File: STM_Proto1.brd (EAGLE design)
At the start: 160 x 100 mm, 81 parts, among them IC1 LM358D, Q1 8M, Q2 32748

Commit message: Libraries for Simholder and HM-10
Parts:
- removed SV1: (no value), con-lstb:MA03-1
- removed U$1: SIMHOLDER3, SparkFun-Connectors:SIMHOLDER3
- added E1: HM-10-BOARD, JNHuaMao:26.9X13X2.2_BOARD
- added LED4: (no value), led:CHIPLED_1206
- added R26, R27: 470, resistor:R0805
- added R28: reset, resistor:R1206
- added U$3: SIMHOLDER3, SparkFun-Connectors:SIMHOLDER3
- moved IC1 97.8 mm to (-24.1, 63.5)
- moved LED1 77.7 mm to (-94.0, 102.9)
- moved C18 71.4 mm to (-16.5, 99.1)
- moved C19 71.4 mm to (-21.6, 99.1)
- moved C10 10.2 mm to (-72.4, 92.7)
- moved R2 10.2 mm to (-47.0, 99.1)
- moved R4 10.2 mm to (-52.1, 99.1)
- moved T1 10.2 mm to (-66.0, 97.8)
- moved T2 10.2 mm to (-71.1, 97.8)
- moved R18 10.2 mm to (-26.7, 99.1)
- moved R3 10.2 mm to (-31.8, 99.1)
- moved C14 10.2 mm to (-77.5, 92.7)
- moved C15 10.2 mm to (-82.5, 92.7)
- moved C16 10.2 mm to (-87.6, 92.7)
- moved C17 10.2 mm to (-92.7, 92.7)
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- renumbered JP2 to JP1
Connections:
- removed net +3V3: SV1.3
- removed net A0.0+: IC1.1, R25.1, SV1.1
- removed net ADC_RES: STM32L152CBT6.18
- new net ADC_TERM: IC1.1, R25.1, STM32L152CBT6.18
- new net I2C_SCL: JP1.3, STM32L152CBT6.42
- new net I2C_SDA: JP1.4, STM32L152CBT6.43
- new net N$26: E1.24, R26.2
- new net N$27: LED4.A, R26.1
- new net N$37: E1.23, R27.2, R28.2
- net 3.3V: now also E1.12, JP1.1, R27.1
- net CTS: no longer JP1.1
- net DCD: no longer JP1.4
- net DTR: no longer JP1.3
- net GND: now also E1.13, E1.14, E1.21, E1.22, JP1.2, LED4.C, R28.1, U$3.6; no longer SV1.2, U$1.6
- net N$10: now also U$3.1; no longer U$1.1
- net N$14: now also U$3.2; no longer U$1.2
- net N$16: now also U$3.3; no longer U$1.3
- net N$18: now also U$3.4; no longer U$1.4
- net RTS: no longer JP1.2
- net USART2_RX: now also E1.1
- net USART2_TX: now also E1.2

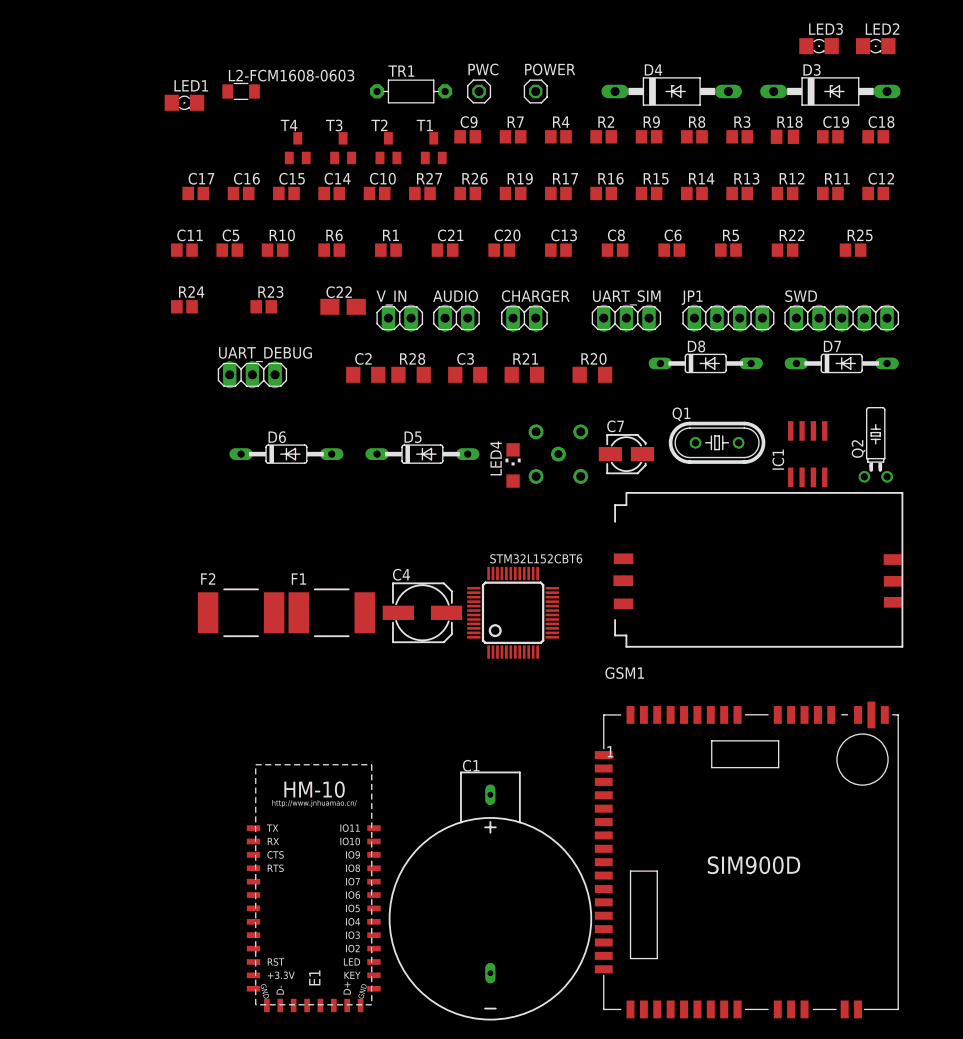
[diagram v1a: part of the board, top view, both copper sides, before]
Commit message: Add Charger
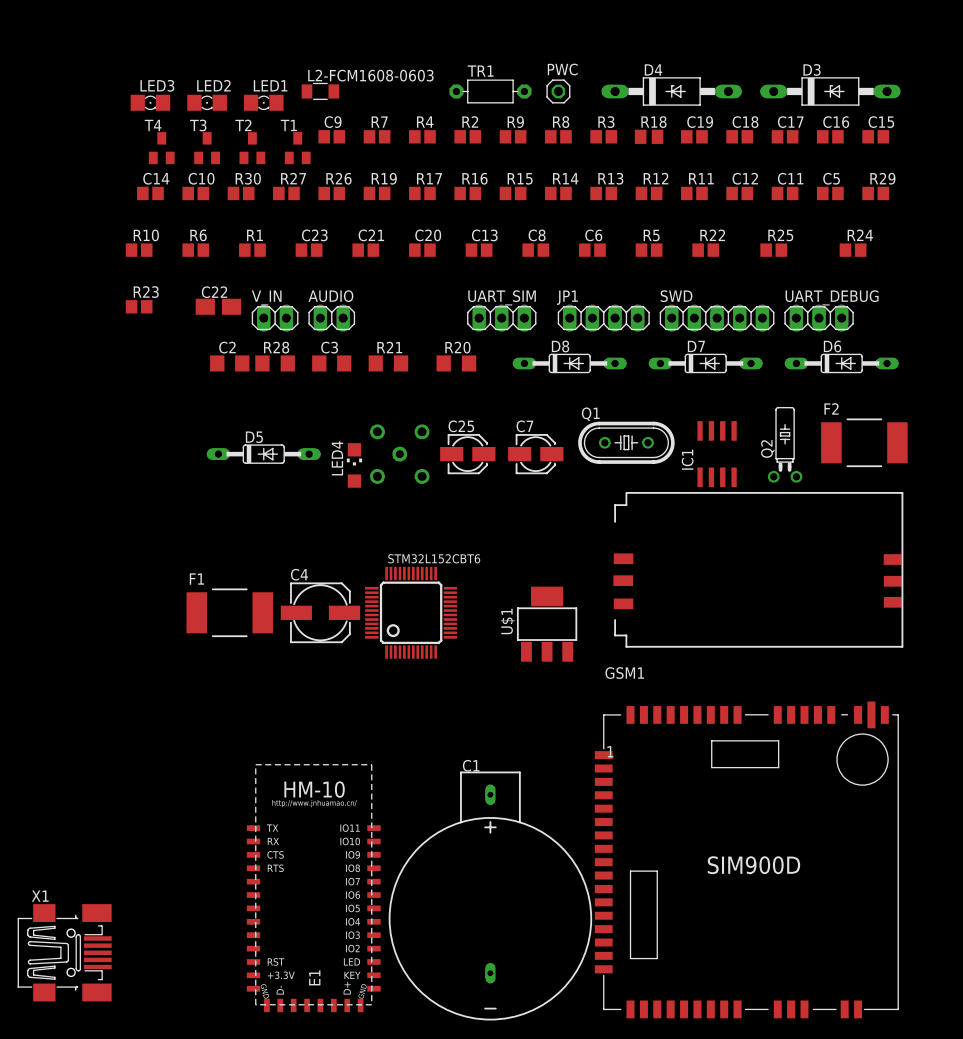
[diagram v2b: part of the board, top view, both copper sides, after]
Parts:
- removed CHARGER: (no value), pinhead:1X02
- removed POWER: (no value), pinhead:1X01
- added C23: 100n, resistor:C0805
- added C25: 10u, resistor:153CLV-0405
- added R29: 4.7k, resistor:R0805
- added R30: 15k, resistor:R0805
- added U$1: LD1117AS33, LD1117AS33:SOT223
- added X1: MINI-USB-32005-201, con-cypressindustries:32005-201
- moved LED3 75.2 mm to (-97.8, 102.9)
- moved R24 75.2 mm to (-19.1, 86.4)
- moved LED2 75.2 mm to (-91.4, 102.9)
- moved F2 72.4 mm to (-17.8, 64.8)
- moved C11 67.6 mm to (-26.7, 92.7)
- moved C5 67.6 mm to (-21.6, 92.7)
- moved C15 66.3 mm to (-16.5, 99.1)
- moved C16 66.3 mm to (-21.6, 99.1)
- moved C17 66.3 mm to (-26.7, 99.1)
- moved UART_DEBUG 63.8 mm to (-22.9, 78.7)
- moved D6 63.1 mm to (-20.3, 73.7)
- moved C14 20.3 mm to (-97.8, 92.7)
- moved C10 20.3 mm to (-92.7, 92.7)
- moved LED4 17.8 mm to (-74.9, 62.2)
- moved D5 17.8 mm to (-85.1, 63.5)
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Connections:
- removed net N$21: CHARGER.2, GSM1.28
- removed net N$6: POWER.1, R10.1
- new net ADC_BAT: R29.2, R30.1, STM32L152CBT6.19
- new net POWER: R10.1, STM32L152CBT6.14
- new net USB+: GSM1.28, X1.1
- net 3.3V: now also C25.+, LED1.A, LED2.A, R16.2, T4.E, U$1.2, U$1.TAB; no longer V_IN.1
- net GND: now also C23.2, C25.-, R30.2, U$1.1, X1.5
- net N$20: no longer CHARGER.1
- net V_IN: now also C23.1, R29.1, U$1.3, V_IN.1; no longer LED1.A, LED2.A, R16.2, T4.E

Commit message: Last version with SIM900D
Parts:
- removed AUDIO: (no value), pinhead:1X02
- removed C18, C19: 33p, resistor:C0805
- removed C22: 1u, resistor:A/3216-18W
- removed C23: 100n, resistor:C0805
- removed C25: 10u, resistor:153CLV-0405
- removed C4: 100u, resistor:153CLV-0605
- removed D3, D4: (no value), diode:F126Z12
- removed E1: HM-10-BOARD, JNHuaMao:26.9X13X2.2_BOARD
- removed JP1: (no value), pinhead:1X04
- removed LED4: (no value), led:CHIPLED_1206
- removed PWC: (no value), pinhead:1X01
- removed R28: reset, resistor:R1206
- removed U$1: LD1117AS33, LD1117AS33:SOT223
- added I2C1, I2C2, I2C3: (no value), pinhead:1X04
- added LED10: (no value), led:CHIPLED_1206
- added R31: 10k, resistor:M0805
- added R31-TEMP: NCP15XH103F03RC, resistor:M0805
- added R32: 10, resistor:M0805
- added R33: RESET_HC, resistor:M0805
- added S1: SWS002, smd-special:SMS-002
- added U$4: (no value), hc-05 eagle lib:BTM400_6B
- added U$5: MIC29302WT, MIC29302WT:TO263-5
- added V_IN1: (no value), pinhead:1X02
- C14: value 10p -> 100u; device resistor:C0805 -> resistor:153CLV-0807
- C15: value 33p -> 22u; device resistor:C0805 -> resistor:153CLV-0605
- C16, C17: value 10p -> 10u; device resistor:C0805 -> resistor:153CLV-0505
- C3: device resistor:C1206 -> resistor:C0805
- C7: value 10u -> 1u
- R26, R27: value 470 -> 4.7k
- moved R23 192.4 mm to (88.2, 35.6), flipped to the bottom, turned to 180 degrees
- moved C14 178.2 mm to (79.3, 72.7), flipped to the bottom
- moved C10 177.5 mm to (74.3, 32.6), flipped to the bottom
- moved L2-FCM1608-0603 174.7 mm to (74.7, 20.5), flipped to the bottom, turned to 270 degrees
- moved F1 173.0 mm to (83.1, 27.7), flipped to the bottom, turned to 270 degrees
- moved R10 170.0 mm to (57.6, 20.4), flipped to the bottom, turned to 270 degrees
- moved C9 167.1 mm to (74.3, 29.0), flipped to the bottom
- moved C21 162.0 mm to (78.0, 29.4), flipped to the bottom, turned to 90 degrees
- moved R27 160.0 mm to (74.9, 64.4), flipped to the bottom, turned to 270 degrees
- moved R26 158.5 mm to (78.5, 64.4), flipped to the bottom, turned to 90 degrees
- moved T3 154.7 mm to (63.0, 87.9), flipped to the bottom
- moved R5 144.3 mm to (88.5, 24.8), flipped to the bottom, turned to 270 degrees
- moved TR1 139.0 mm to (69.8, 53.5), turned to 270 degrees
- moved T4 138.6 mm to (41.1, 81.2), flipped to the bottom
- moved LED3 136.9 mm to (37.7, 83.7), flipped to the bottom, turned to 270 degrees
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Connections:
- removed net N$26: E1.24, R26.2
- removed net N$27: LED4.A, R26.1
- removed net N$37: E1.23, R27.2, R28.2
- removed net N$7: GSM1.47, PWC.1
- new net N$21: R32.1, U$4.PIO(1)
- new net N$33: LED10.A, R32.2
- new net N$38: R26.2, R27.1, U$5.5
- new net N$6: R31.1, R33.1, U$4.RESETB
- new net VBAT@2: GSM1.38, GSM1.39, S1.1, S1.2
- net 3.3V: now also C14.+, C15.+, C16.+, I2C1.1, I2C2.1, I2C3.1, R26.1, R31.2, S1.4, U$4.3.3V, U$5.4, V_IN1.1; no longer C25.+, C4.+, C7.+, E1.12, GSM1.38, GSM1.39, JP1.1, R27.1, U$1.2, U$1.TAB
- net GND: now also C14.-, C15.-, C16.-, C17.-, I2C1.2, I2C2.2, I2C3.2, LED10.C, R27.2, R31-TEMP.2, R33.2, U$4.GND@1, U$4.GND@2, U$4.GND@3, U$4.GND@4, U$5.3, V_IN1.2; no longer C14.1, C15.1, C17.2, C18.2, C22.-, C23.2, C25.-, C4.-, D3.C, D4.A, E1.13, E1.14, E1.21, E1.22, JP1.2, LED4.C, R28.1, U$1.1
- net I2C_SCL: now also I2C1.3, I2C2.3, I2C3.3; no longer JP1.3
- net I2C_SDA: now also I2C1.4, I2C2.4, I2C3.4; no longer JP1.4
- net N$20: now also R31-TEMP.1
- net N$31: now also C7.+; no longer C22.+
- net OUT+: no longer AUDIO.2, C16.2, C17.1, C18.1, C19.2, D4.C
- net OUT-: no longer AUDIO.1, C14.2, C15.2, C16.1, C19.1, D3.A
- net USART2_RX: now also U$4.UART-RX; no longer E1.1
- net USART2_TX: now also U$4.UART-TX; no longer E1.2
- net V_IN: now also C17.+, S1.3, U$5.1, U$5.2; no longer C23.1, U$1.3
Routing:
- net GND: track 0.00 -> 803.2 mm, vias 0 -> 6
- net 3.3V: track 0.00 -> 505.1 mm, vias 0 -> 10
- net V_IN: track 0.00 -> 348.0 mm, vias 0 -> 4
- net USART2_TX: track 0.00 -> 332.7 mm, vias 0 -> 4
- net USART2_RX: track 0.00 -> 325.2 mm, vias 0 -> 2
- net N$1: track 0.00 -> 201.5 mm, vias 0 -> 2
- net NRST: track 0.00 -> 129.2 mm, vias 0 -> 6
- net DEB_TX: track 0.00 -> 128.4 mm
- net DEB_RX: track 0.00 -> 108.1 mm
- net PWRK: track 0.00 -> 93.5 mm
- net ADC_BAT: track 0.00 -> 87.8 mm
- net I2C_SDA: track 0.00 -> 85.3 mm, vias 0 -> 4
- net RING: track 0.00 -> 84.4 mm
- net I2C_SCL: track 0.00 -> 82.7 mm, vias 0 -> 4
- net N$10: track 0.00 -> 82.1 mm
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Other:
- board size 160 x 100 mm -> 113.2 x 103.6 mm
